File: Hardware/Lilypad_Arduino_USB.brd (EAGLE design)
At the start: 50.8 x 50.8 mm, 44 parts, among them U1 MCP73831, U2 MIC5219, U3 ATMEGA32U4QFN, X1 USB-MICROB, Y1 8MHz

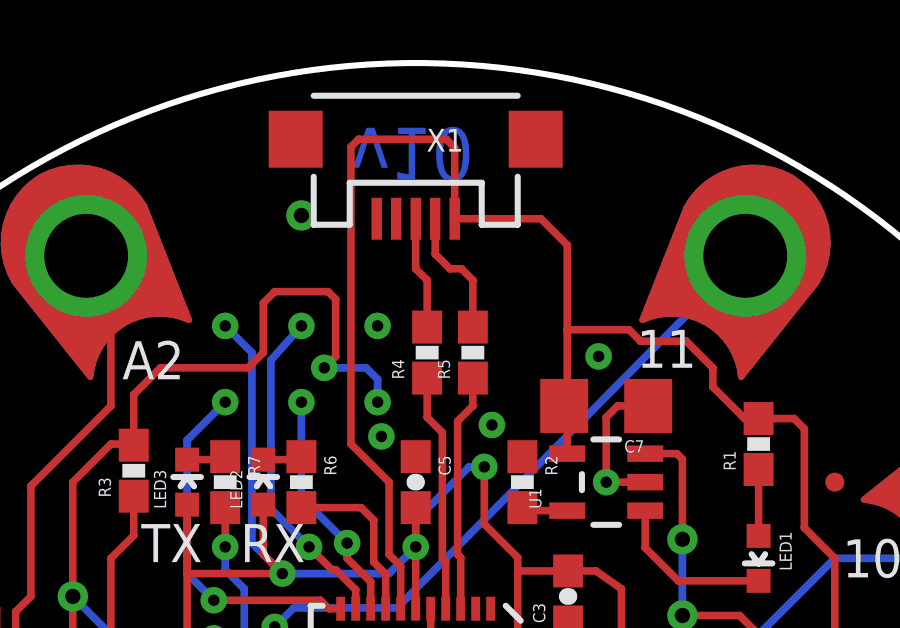
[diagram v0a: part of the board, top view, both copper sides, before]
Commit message: Change micro USB connector to more robust package.
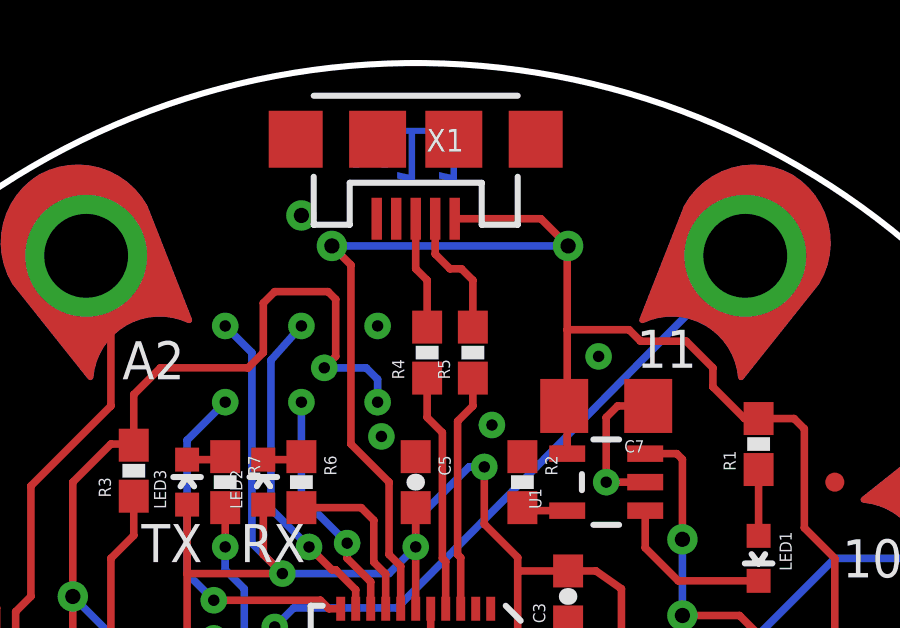
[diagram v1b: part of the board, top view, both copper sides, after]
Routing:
- net 5V: track 90.1 -> 88.9 mm, vias 2 -> 4
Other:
- board text added: "v11"
- board text removed: "v10"
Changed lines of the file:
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@@
 <layer number="144" name="Drill_legend" color="7" fill="1" visible="no" active="no"/>
 <layer number="151" name="HeatSink" color="7" fill="1" visible="no" active="no"/>
+<layer number="199" name="Contour" color="7" fill="1" visible="yes" active="yes"/>
 <layer number="200" name="200bmp" color="1" fill="10" visible="no" active="no"/>
 <layer number="201" name="201bmp" color="2" fill="1" visible="no" active="no"/>
@@
 <text x="-0.634996875" y="-18.922996875" size="1.6764" layer="21" font="vector" ratio="15">+</text>
 <text x="-9.651996875" y="-16.509996875" size="1.6764" layer="21" font="vector" ratio="15">-</text>
-<text x="-2.158996875" y="23.240996875" size="1.778" layer="16" font="vector" ratio="15" rot="SMR180">v10</text>
+<text x="-2.158996875" y="23.240996875" size="1.778" layer="16" font="vector" ratio="15" rot="SMR180">v11</text>
 <circle x="0" y="0" radius="25.4" width="0.2032" layer="20"/>
 <polygon width="0.254" layer="29">
@@
 <wire x1="-0.5" y1="7.209996875" x2="-0.499996875" y2="8.627996875" width="0.254" layer="1"/>
 <wire x1="-0.499996875" y1="8.627996875" x2="-0.888996875" y2="9.016996875" width="0.254" layer="1"/>
-<wire x1="-2.159" y1="22.60599375" x2="-1.904996875" y2="22.859996875" width="0.254" layer="1"/>
-<wire x1="-1.904996875" y1="22.859996875" x2="1.016" y2="22.859996875" width="0.254" layer="1"/>
-<wire x1="1.016" y1="22.859996875" x2="1.3" y2="22.575996875" width="0.254" layer="1"/>
-<wire x1="1.3" y1="20.209996875" x2="1.3" y2="22.575996875" width="0.254" layer="1"/>
 <wire x1="11.429996875" y1="13.549996875" x2="10.961" y2="13.549996875" width="0.254" layer="1"/>
 <wire x1="10.961" y1="13.549996875" x2="9.906" y2="14.604996875" width="0.254" layer="1"/>
@@
 <wire x1="9.906" y1="15.239996875" x2="9.017" y2="16.128996875" width="0.254" layer="1"/>
 <wire x1="-0.888996875" y1="9.016996875" x2="-0.888996875" y2="11.429996875" width="0.254" layer="1"/>
-<wire x1="-2.158996875" y1="12.699996875" x2="-2.159" y2="22.60599375" width="0.254" layer="1"/>
+<wire x1="-2.158996875" y1="12.699996875" x2="-2.159" y2="18.669" width="0.254" layer="1"/>
 <wire x1="-2.158996875" y1="12.699996875" x2="-0.888996875" y2="11.429996875" width="0.254" layer="1"/>
 <wire x1="5.0499" y1="16.509996875" x2="7.112" y2="16.509996875" width="0.254" layer="1"/>
@@
 <wire x1="5.0499" y1="13.870096875" x2="5.0499" y2="16.509996875" width="0.254" layer="1"/>
 <wire x1="5.0499" y1="16.509996875" x2="5.0499" y2="19.334096875" width="0.254" layer="1"/>
+<wire x1="5.0499" y1="19.334096875" x2="5.049903125" y2="19.334096875" width="0.254" layer="1"/>
+<wire x1="5.049903125" y1="19.334096875" x2="5.08" y2="19.304" width="0.254" layer="1"/>
+<via x="5.08" y="19.304" extent="1-16" drill="0.508"/>
+<wire x1="5.08" y1="19.304" x2="-2.794" y2="19.304" width="0.254" layer="16"/>
+<via x="-2.794" y="19.304" extent="1-16" drill="0.508"/>
+<wire x1="-2.794" y1="19.304" x2="-2.159" y2="18.669" width="0.254" layer="1"/>
 </signal>
 <signal name="N$19">

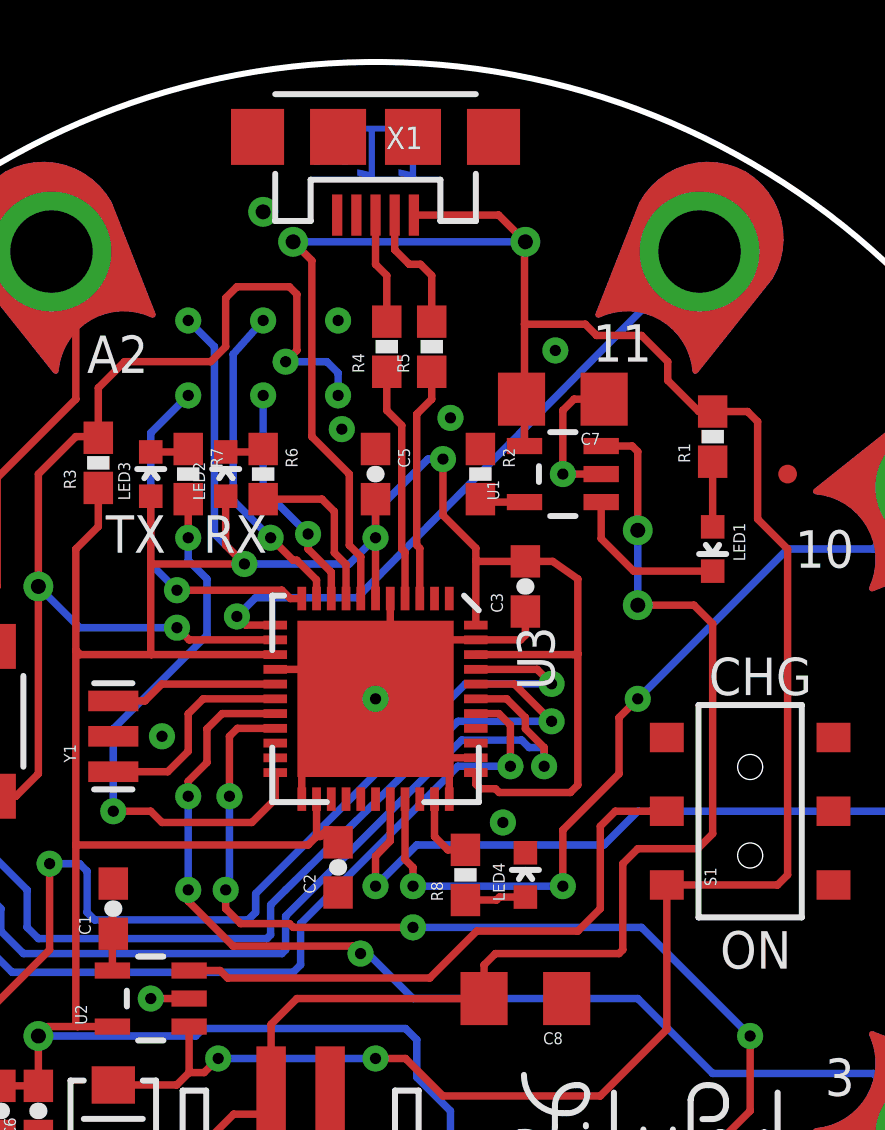
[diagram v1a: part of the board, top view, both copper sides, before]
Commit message: Changed version number in both files.
Masked via at .35, .275 to provide a test point for the charge circuit.
Add USR mask on the user control LED to make it more clear what it does.

Closes issues 1 and 2.
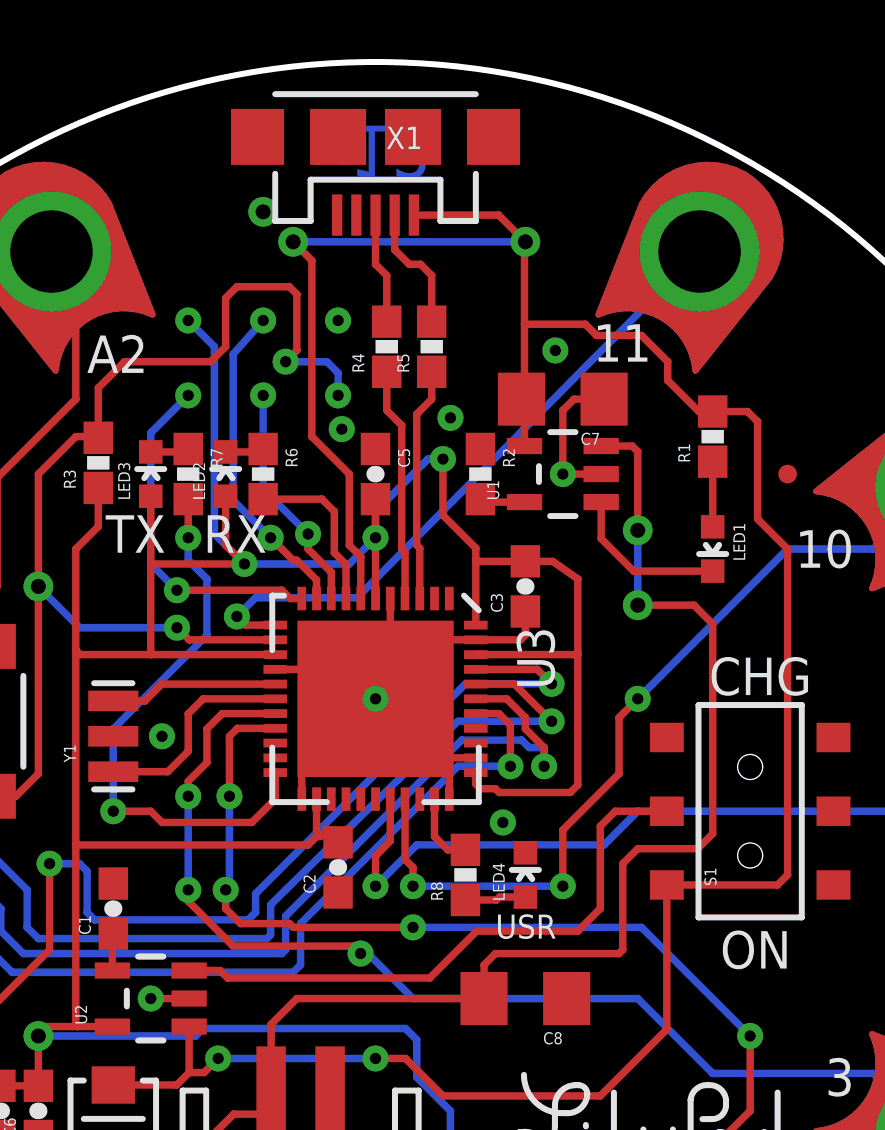
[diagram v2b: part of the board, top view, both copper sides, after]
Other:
- board text added: "USR"
- board text added: "v12"
- board text removed: "v11"
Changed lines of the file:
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@@
 <layer number="28" name="bValues" color="7" fill="1" visible="no" active="yes"/>
 <layer number="29" name="tStop" color="7" fill="3" visible="no" active="yes"/>
-<layer number="30" name="bStop" color="7" fill="6" visible="no" active="yes"/>
+<layer number="30" name="bStop" color="7" fill="6" visible="yes" active="yes"/>
 <layer number="31" name="tCream" color="7" fill="4" visible="no" active="yes"/>
 <layer number="32" name="bCream" color="7" fill="5" visible="no" active="yes"/>
@@
 <layer number="144" name="Drill_legend" color="7" fill="1" visible="no" active="no"/>
 <layer number="151" name="HeatSink" color="7" fill="1" visible="no" active="no"/>
-<layer number="199" name="Contour" color="7" fill="1" visible="yes" active="yes"/>
+<layer number="199" name="Contour" color="7" fill="1" visible="no" active="no"/>
 <layer number="200" name="200bmp" color="1" fill="10" visible="no" active="no"/>
 <layer number="201" name="201bmp" color="2" fill="1" visible="no" active="no"/>
@@
 <text x="-0.634996875" y="-18.922996875" size="1.6764" layer="21" font="vector" ratio="15">+</text>
 <text x="-9.651996875" y="-16.509996875" size="1.6764" layer="21" font="vector" ratio="15">-</text>
-<text x="-2.158996875" y="23.240996875" size="1.778" layer="16" font="vector" ratio="15" rot="SMR180">v11</text>
+<text x="-2.158996875" y="23.240996875" size="1.778" layer="16" font="vector" ratio="15" rot="SMR180">v12</text>
 <circle x="0" y="0" radius="25.4" width="0.2032" layer="20"/>
 <polygon width="0.254" layer="29">
@@
 <vertex x="-3.19656875" y="-25.090384375"/>
 </polygon>
+<circle x="8.89" y="6.985" radius="0.40160625" width="0.254" layer="30"/>
+<text x="4.064" y="-4.318" size="0.8128" layer="21" font="vector" ratio="15">USR</text>
 </plain>
 <attributes>

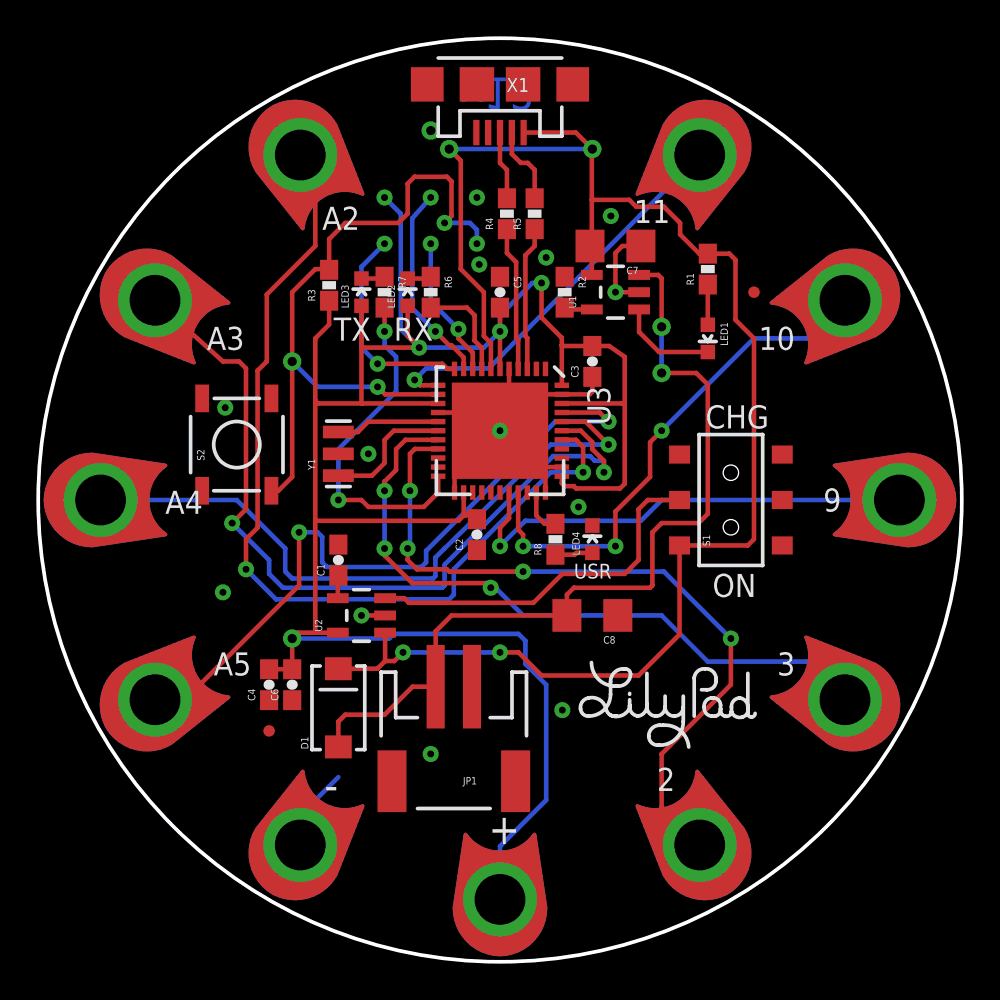
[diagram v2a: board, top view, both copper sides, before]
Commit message: Quality Control Revision to PCB layout
Changed:
- Updated all 0402 footprints to 0603
- Updated with new 1:1 footprint of 32u4 IC
- Rerouted all traces straight away from IC
- Added trestrict under IC to mitigate gnd plane
- Moved crystal closer to IC
- Updated microUSB footprint for new production part
- Added test point for charge circuit
- Updated version number in bottom copper and schematic
- Added silk for charge and stat LEDs
- Added gnd vias to mitigate orphaned pours
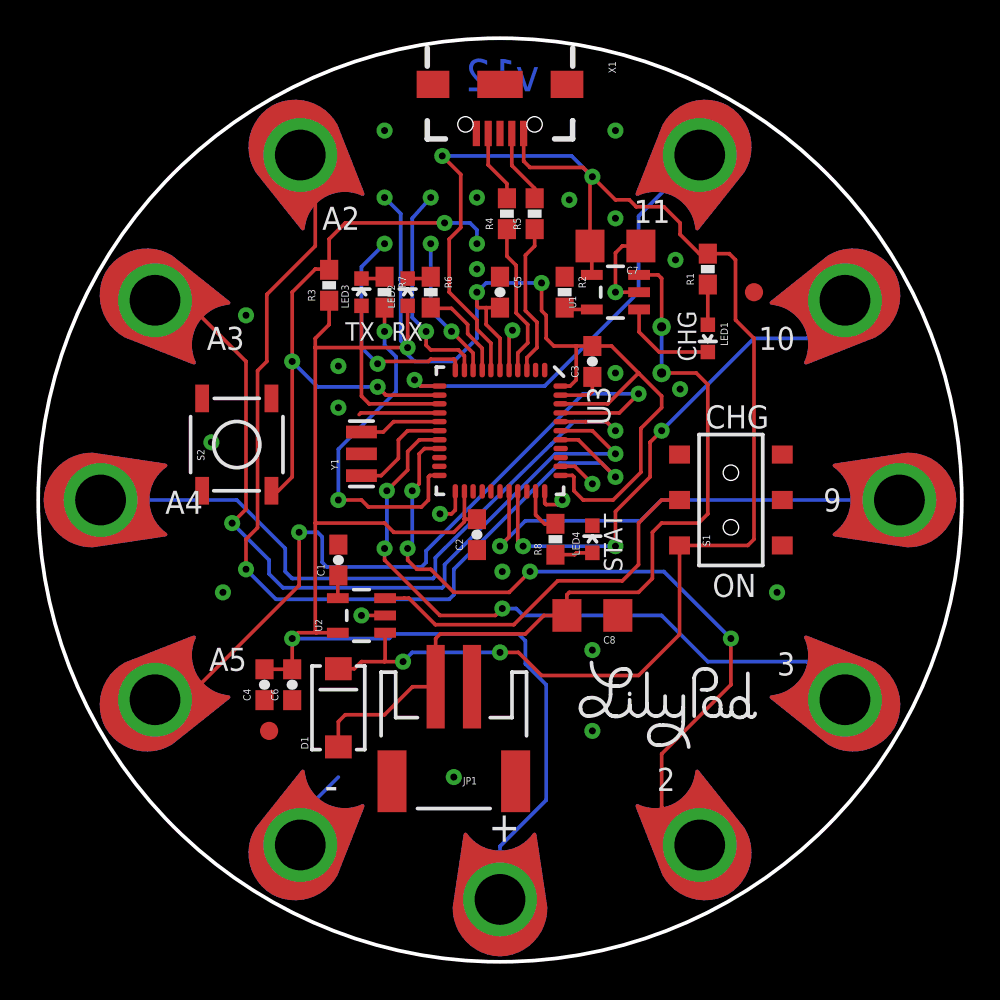
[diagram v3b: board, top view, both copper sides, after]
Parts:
- added U$5: OSHW-LOGOM, SparkFun:OSHW-LOGO-M
- JP2, JP3: value FIDUCIALUFIDUCIAL -> FIDUCIAL1X2; device SparkFun:MICRO-FIDUCIAL -> SparkFun:FIDUCIAL-1X2
- R2, R3, R4, R5, R6: device SparkFun-Passives:0603-RES -> SparkFun-Resistors:0603-RES
- U3: value ATMEGA32U4QFN -> ATMEGA32U41:1; device SparkFun-DigitalIC:QFN-44 -> Testing:QFN-44-NOPAD_1:1
- X1: value USB-MICROB -> (none); device SparkFun-Connectors:USB-MICROB -> Testing:USB-AB-MICRO-SMD_V03
- moved Y1 1.27 mm to (-7.62, 2.54)
- moved C4 0.25 mm to (-13.0, -10.2)
- turned X1 to 270 degrees
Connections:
- new net N$22: X1.D+1
- net 5V: now also X1.VBUS1; no longer X1.VBUS
- net GND: now also X1.GND1; no longer U3.EPAD, X1.GND, X1.MT1, X1.MT2
- net N$19: now also X1.D-1; no longer X1.D-
- net N$20: now also X1.ID1; no longer X1.D+
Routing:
- net GND: track 38.2 -> 26.1 mm, vias 14 -> 25
- net 3.3V: track 127.3 -> 136.6 mm
- net RESET: track 39.0 -> 34.2 mm
- net N$14: track 38.9 -> 43.1 mm
- net N$17: track 50.5 -> 53.9 mm
- net N$9: track 22.3 -> 25.0 mm
- net 5V: track 88.9 -> 90.6 mm
- net N$5: track 7.26 -> 5.90 mm
- net N$15: track 37.2 -> 38.4 mm
- net N$7: track 5.73 -> 4.52 mm
- net MOSI: track 11.1 -> 12.0 mm
- net N$12: track 40.9 -> 41.6 mm
- net N$2: track 20.3 -> 21.0 mm
- net MISO: track 11.8 -> 12.4 mm
- net D-: track 7.94 -> 8.45 mm
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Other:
- board text added: "STAT"
- board text removed: "USR"
